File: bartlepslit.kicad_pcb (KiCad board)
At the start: 2 copper layers, 336.7 x 119.6 mm, 119 parts, among them K1 SW_Push, K10 SW_Push, K11 SW_Push, K12 SW_Push, K13 SW_Push, K14 SW_Push, K15 SW_Push, K16 SW_Push, K17 SW_Push, K18 SW_Push, K19 SW_Push, K2 SW_Push, K20 SW_Push, K21 SW_Push, K22 SW_Push, K23 SW_Push, K24 SW_Push, K25 SW_Push, K26 SW_Push, K27 SW_Push, K28 SW_Push, K29 SW_Push, K3 SW_Push, K30 SW_Push, K31 SW_Push, K32 SW_Push, K33 SW_Push, K34 SW_Push, K35 SW_Push, K36 SW_Push, K37 SW_Push, K38 SW_Push, K39 SW_Push, K4 SW_Push, K40 SW_Push, K41 SW_Push, K42 SW_Push, K5 SW_Push, K6 SW_Push, K7 SW_Push, K8 SW_Push, K9 SW_Push, U1 ProMicro

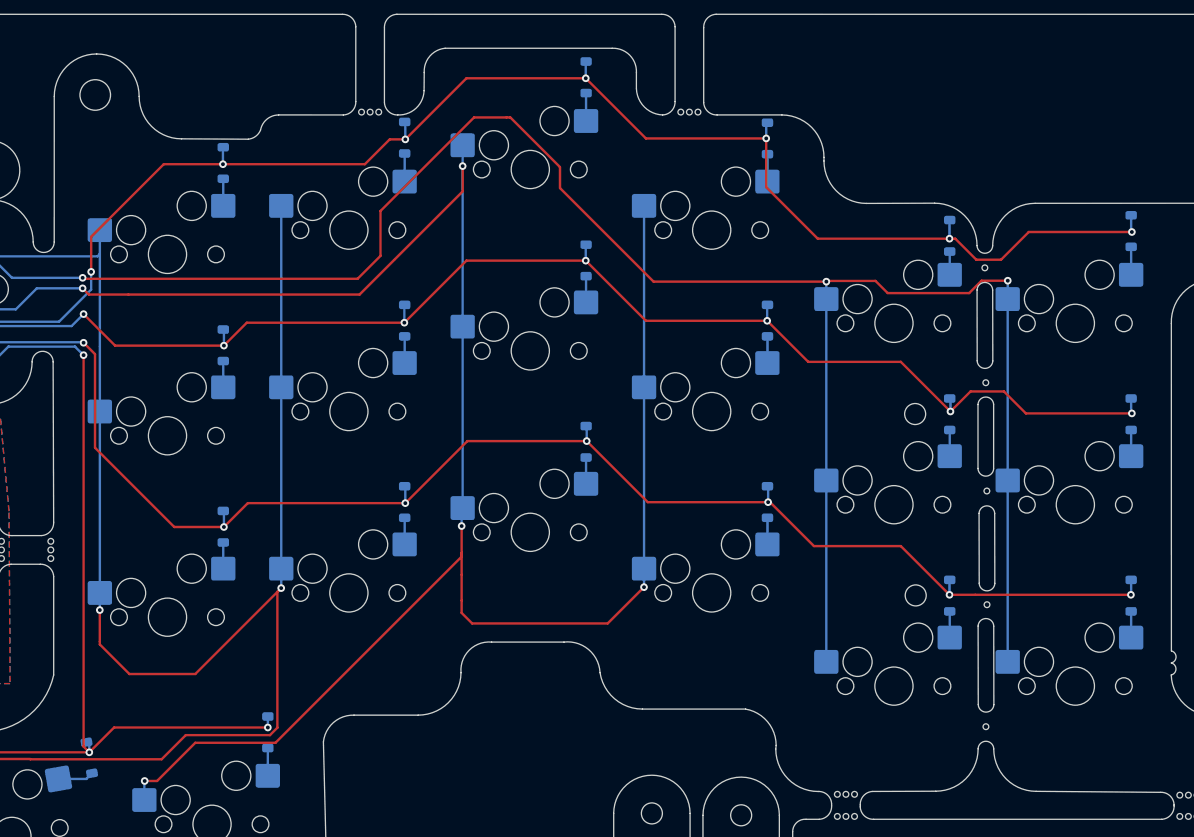
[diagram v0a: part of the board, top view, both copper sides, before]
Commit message: feat: fixed orientation of diodes
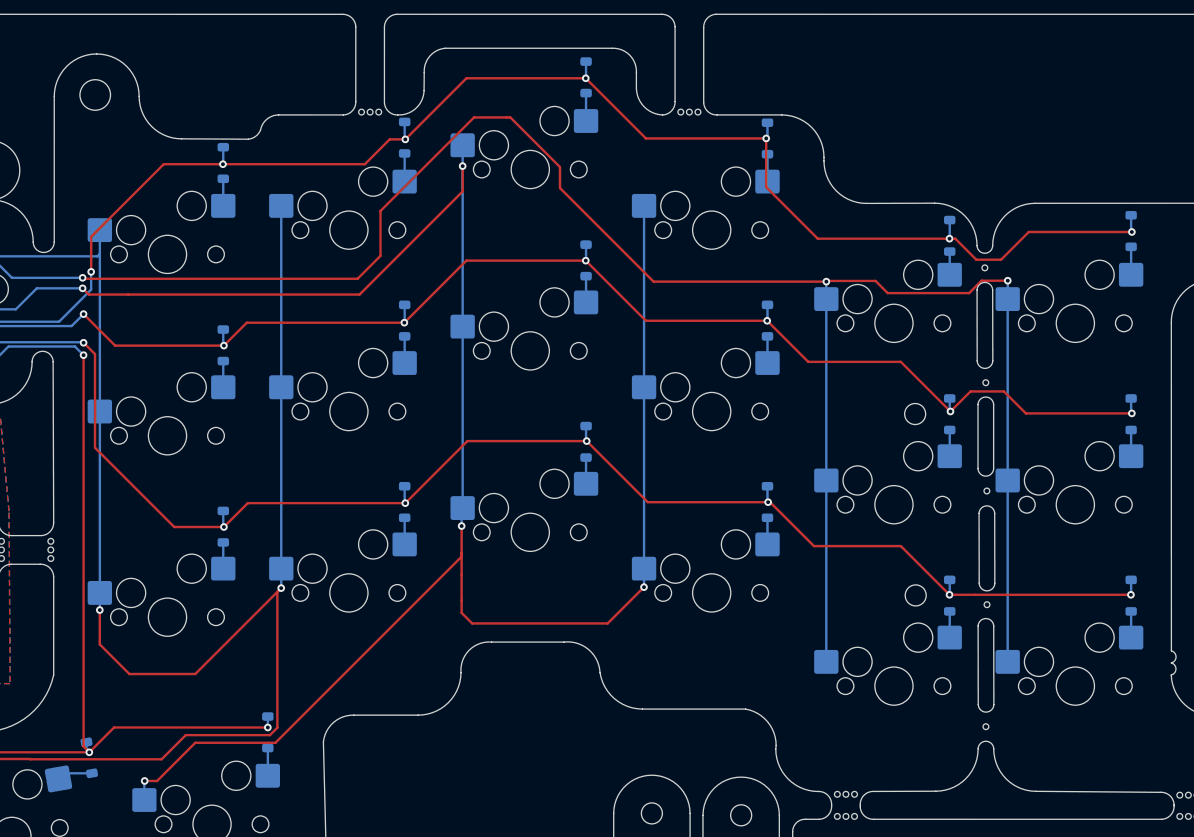
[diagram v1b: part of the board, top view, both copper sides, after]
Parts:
- turned D19 to 90 degrees
- turned D20 to 90 degrees
- turned D21 to 90 degrees
- turned D22 to -90 degrees
- turned D23 to -90 degrees
- turned D24 to -90 degrees
- turned D25 to 90 degrees
- turned D26 to 90 degrees
- turned D27 to 90 degrees
- turned D28 to -90 degrees
- turned D29 to -90 degrees
- turned D30 to -90 degrees
- turned D31 to 90 degrees
- turned D32 to 90 degrees
- turned D33 to 90 degrees
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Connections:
- D19 pad 1: ROW_1 -> Net-(D19-K)
- D19 pad 2: Net-(D19-A) -> ROW_1
- D20 pad 1: ROW_2 -> Net-(D20-K)
- D20 pad 2: Net-(D20-A) -> ROW_2
- D21 pad 1: ROW_3 -> Net-(D21-K)
- D21 pad 2: Net-(D21-A) -> ROW_3
- D22 pad 1: Net-(D22-K) -> ROW_1
- D22 pad 2: ROW_1 -> Net-(D22-A)
- D23 pad 1: Net-(D23-K) -> ROW_2
- D23 pad 2: ROW_2 -> Net-(D23-A)
- D24 pad 1: Net-(D24-K) -> ROW_3
- D24 pad 2: ROW_3 -> Net-(D24-A)
- D25 pad 1: ROW_1 -> Net-(D25-K)
- D25 pad 2: Net-(D25-A) -> ROW_1
- D26 pad 1: ROW_2 -> Net-(D26-K)
- D26 pad 2: Net-(D26-A) -> ROW_2
- D27 pad 1: ROW_3 -> Net-(D27-K)
- D27 pad 2: Net-(D27-A) -> ROW_3
- D28 pad 1: Net-(D28-K) -> ROW_1
- D28 pad 2: ROW_1 -> Net-(D28-A)
- D29 pad 1: Net-(D29-K) -> ROW_2
- D29 pad 2: ROW_2 -> Net-(D29-A)
- D30 pad 1: Net-(D30-K) -> ROW_3
- D30 pad 2: ROW_3 -> Net-(D30-A)
- D31 pad 1: ROW_1 -> Net-(D31-K)
- D31 pad 2: Net-(D31-A) -> ROW_1
- D32 pad 1: ROW_2 -> Net-(D32-K)
- D32 pad 2: Net-(D32-A) -> ROW_2
- D33 pad 1: ROW_3 -> Net-(D33-K)
- D33 pad 2: Net-(D33-A) -> ROW_3
- D34 pad 1: Net-(D34-K) -> ROW_1
- D34 pad 2: ROW_1 -> Net-(D34-A)
- D35 pad 1: Net-(D35-K) -> ROW_2
- D35 pad 2: ROW_2 -> Net-(D35-A)
- D36 pad 1: Net-(D36-K) -> ROW_3
- D36 pad 2: ROW_3 -> Net-(D36-A)
- K19 pad 2: Net-(D19-A) -> Net-(D19-K)
- K20 pad 2: Net-(D20-A) -> Net-(D20-K)
- K21 pad 2: Net-(D21-A) -> Net-(D21-K)
- K22 pad 2: Net-(D22-K) -> Net-(D22-A)
- K23 pad 2: Net-(D23-K) -> Net-(D23-A)
- K24 pad 2: Net-(D24-K) -> Net-(D24-A)
- K25 pad 2: Net-(D25-A) -> Net-(D25-K)
- K26 pad 2: Net-(D26-A) -> Net-(D26-K)
- K27 pad 2: Net-(D27-A) -> Net-(D27-K)
- K28 pad 2: Net-(D28-K) -> Net-(D28-A)
- K29 pad 2: Net-(D29-K) -> Net-(D29-A)
- K30 pad 2: Net-(D30-K) -> Net-(D30-A)
- K31 pad 2: Net-(D31-A) -> Net-(D31-K)
- K32 pad 2: Net-(D32-A) -> Net-(D32-K)
- K33 pad 2: Net-(D33-A) -> Net-(D33-K)
- K34 pad 2: Net-(D34-K) -> Net-(D34-A)
- K35 pad 2: Net-(D35-K) -> Net-(D35-A)
- K36 pad 2: Net-(D36-K) -> Net-(D36-A)
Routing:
- net Net-(D22-K): track 2.95 -> 0.00 mm
- net Net-(D22-A): track 0.00 -> 2.95 mm
- net Net-(D34-K): track 2.93 -> 0.00 mm
- net Net-(D34-A): track 0.00 -> 2.93 mm
- net Net-(D25-K): track 0.00 -> 2.92 mm
- net Net-(D25-A): track 2.92 -> 0.00 mm
- net Net-(D28-K): track 2.87 -> 0.00 mm
- net Net-(D28-A): track 0.00 -> 2.87 mm
- net Net-(D19-K): track 0.00 -> 2.84 mm
- net Net-(D19-A): track 2.84 -> 0.00 mm
- net Net-(D29-K): track 2.79 -> 0.00 mm
- net Net-(D29-A): track 0.00 -> 2.79 mm
- net Net-(D23-K): track 2.79 -> 0.00 mm
- net Net-(D23-A): track 0.00 -> 2.79 mm
- net Net-(D30-K): track 2.79 -> 0.00 mm
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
